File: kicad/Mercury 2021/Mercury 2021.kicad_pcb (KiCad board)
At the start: 2 copper layers, 100 x 100 mm, 41 parts, among them J1 Batt_Power, J10 3.3v rail, J13 Screw_Terminal_01x02, J14 Screw_Terminal_01x02, J15 Raspberry_Pi_2_3, J16 Sensors_Extra, J17 Arduino_Extra_Power, J18 Arduino_Extra_Comm, J19 Arduino_Extra_Digital, J2 Conn_01x20_Female, J20 Arduino_Extra_Analog, J21 MP_Extra_Analog, J3 Conn_01x20_Female, J30 Screw_Terminal_01x02, J31 Screw_Terminal_01x02, J32 Screw_Terminal_01x02, J33 Screw_Terminal_01x02, J36 GND rail 2, J37 GND rail 3, J4 Screw_Terminal_01x02, J5 Screw_Terminal_01x02, J7 5V rail, J8 GND Rail 1, J9 11v rail, U1 LM1084-5.0, U10 TCA9548APWR, U11 MDD10A, U12 PCA9685, U12C1 PCA9685, U13 MDD10A, U2 Adafruit_VL53L0X, U3 Adafruit_VL53L0X, U4 Adafruit_VL53L0X, U5 Adafruit_VL53L0X, U6 Adafruit_VL53L0X, U7 Adafruit_VL53L0X, U8 Adafruit_VL53L0X, U9 Adafruit_VL53L0X

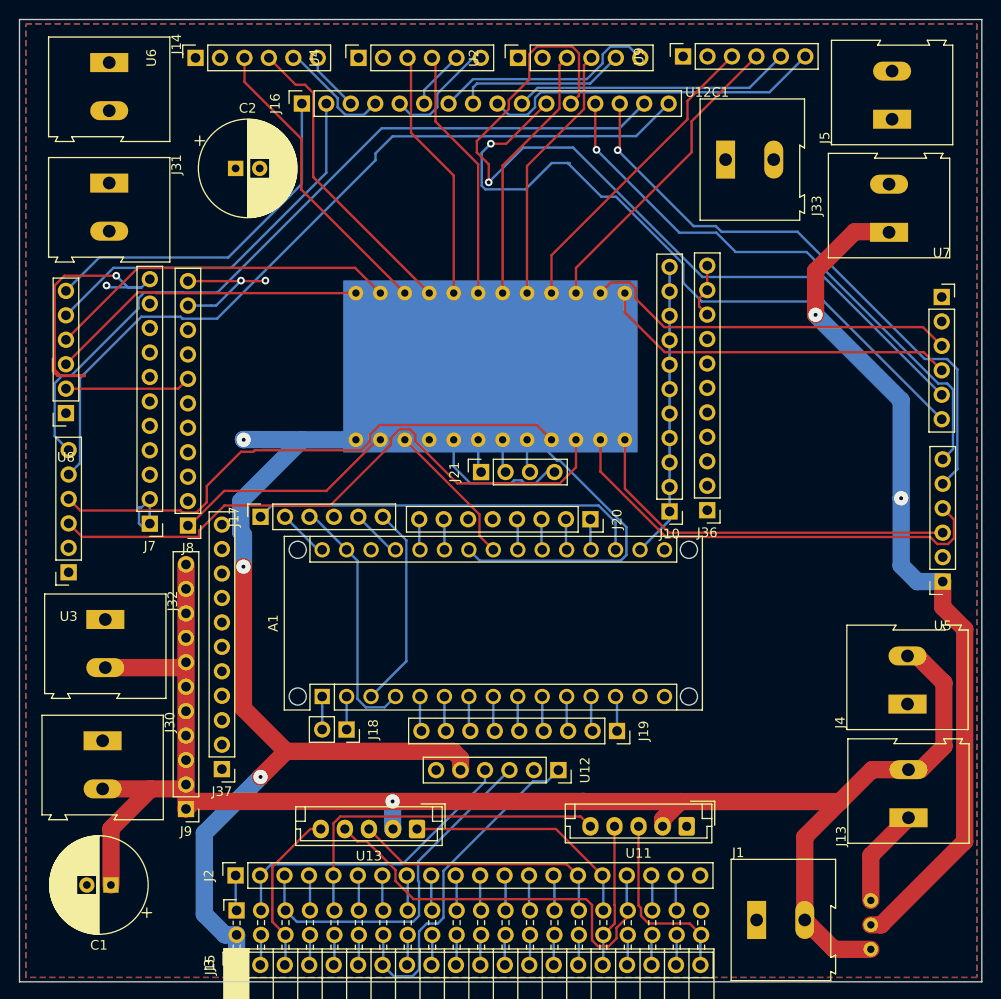
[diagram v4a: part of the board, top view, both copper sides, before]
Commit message: Updated board
Silk screen and mounting holes
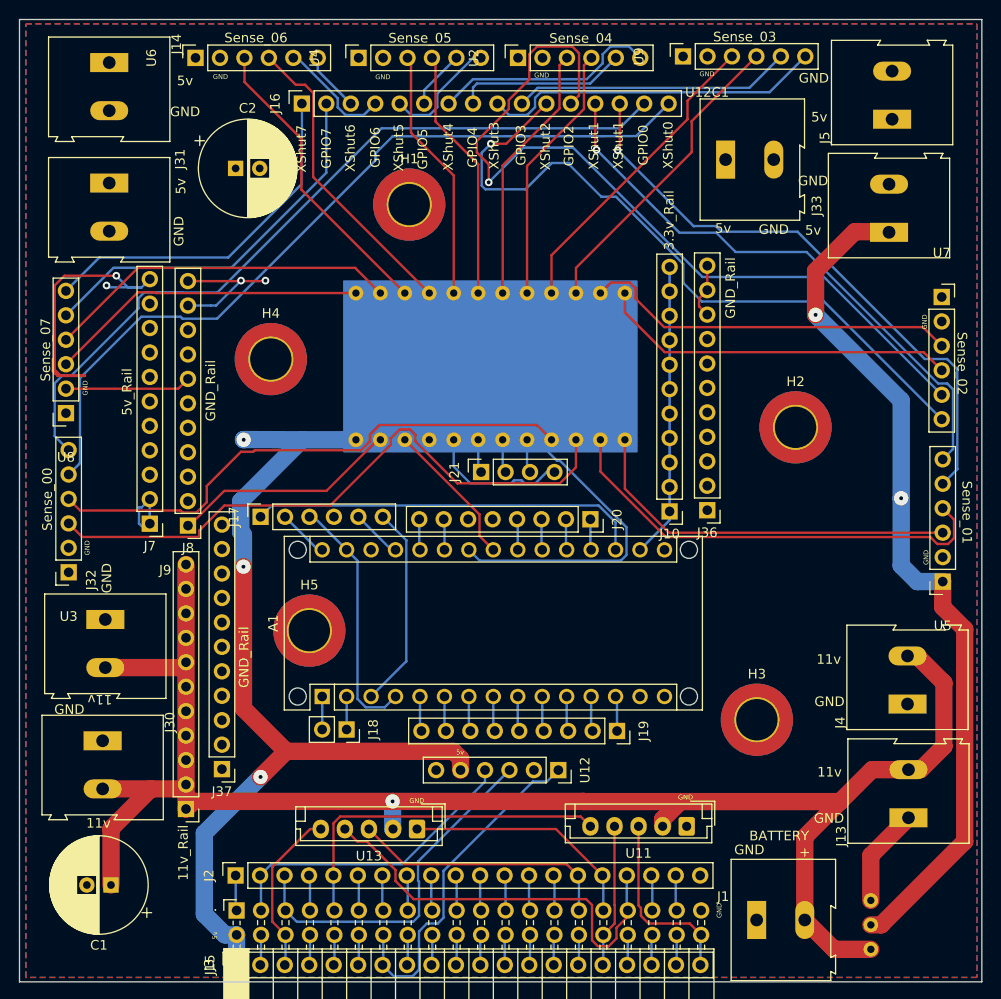
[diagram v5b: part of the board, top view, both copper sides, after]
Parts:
- added H1: MountingHole, MountingHole:MountingHole_4.3mm_M4_DIN965_Pad_TopBottom, F.Cu at (58.6, 38.8)
- added H2: MountingHole, MountingHole:MountingHole_4.3mm_M4_DIN965_Pad_TopBottom, F.Cu at (98.8, 62.0)
- added H3: MountingHole, MountingHole:MountingHole_4.3mm_M4_DIN965_Pad_TopBottom, F.Cu at (94.7, 92.4)
- added H4: MountingHole, MountingHole:MountingHole_4.3mm_M4_DIN965_Pad_TopBottom, F.Cu at (44.2, 54.9)
- added H5: MountingHole, MountingHole:MountingHole_4.3mm_M4_DIN965_Pad_TopBottom, F.Cu at (48.2, 83.1)
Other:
- board text added: "+"
- board text added: "11v"
- board text added: "11v_Rail"
- board text added: "3.3v_Rail"
- board text added: "5v"
- board text added: "5v GND"
- board text added: "5v_Rail"
- board text added: "BATTERY"
- board text added: "Board by: Max Myzer With contributions from: CNC3"
- board text added: "Created in KiCAD"
- board text added: "GND"
- board text added: "GND_Rail"
- board text added: "GPIO0"
- board text added: "GPIO2"
- board text added: "GPIO3"
- board text added: "GPIO4"
- board text added: "GPIO5"
- board text added: "GPIO6"
- board text added: "GPIO7"
- board text added: "KSU Mercury 2021"
- board text added: "Kansas State Robotics Competition Team"
- board text added: "Sense_00"
- board text added: "Sense_01"
- board text added: "Sense_02"
- board text added: "Sense_03"
- board text added: "Sense_04"
- board text added: "Sense_05"
- board text added: "Sense_06"
- board text added: "Sense_07"
- board text added: "XShut0"
- board text added: "XShut1"
- board text added: "XShut2"
- board text added: "XShut3"
- board text added: "XShut4"
- board text added: "XShut5"
- board text added: "XShut6"
- board text added: "XShut7"
- board text added: "https://github.com/ksurct/mercury2021"
- board text added: "•"
